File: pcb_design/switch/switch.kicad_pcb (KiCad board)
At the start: 2 copper layers, 5 parts

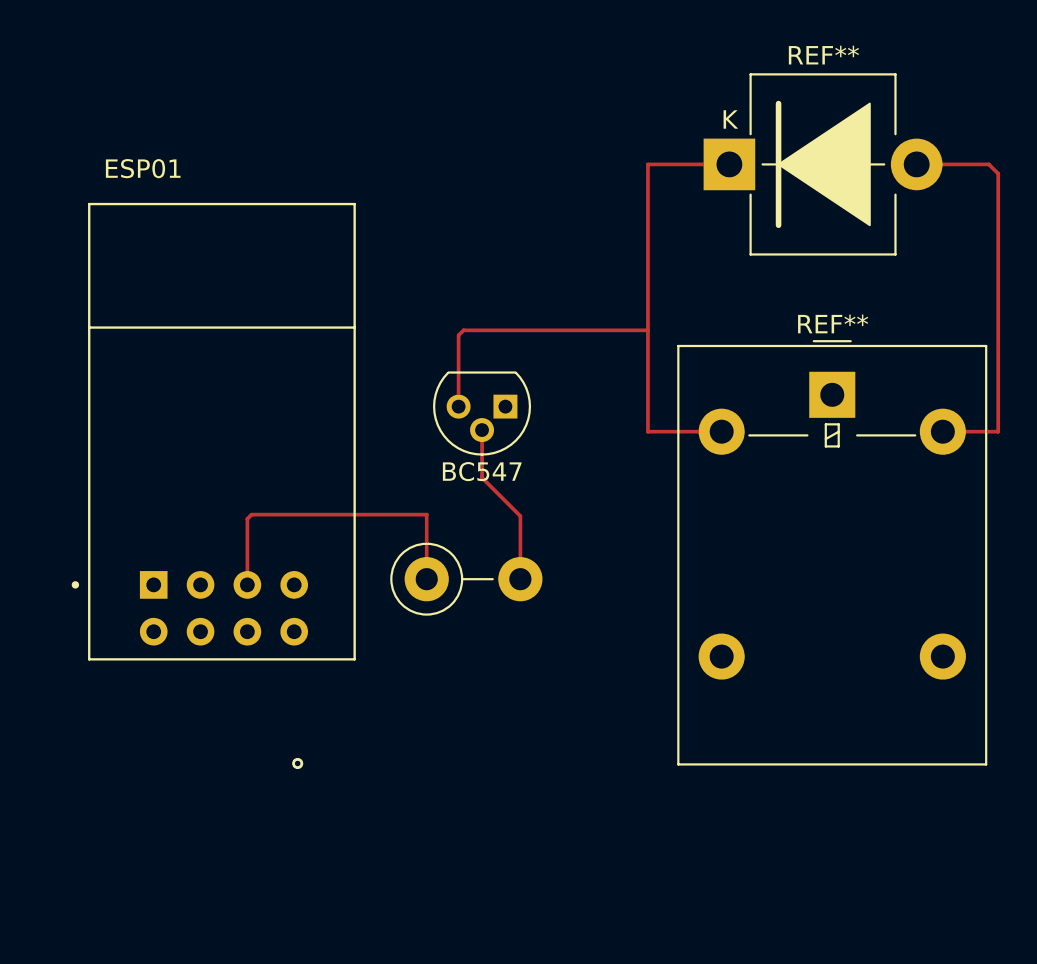
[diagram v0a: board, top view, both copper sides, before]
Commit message: Update fp-info-cache in switch design ``
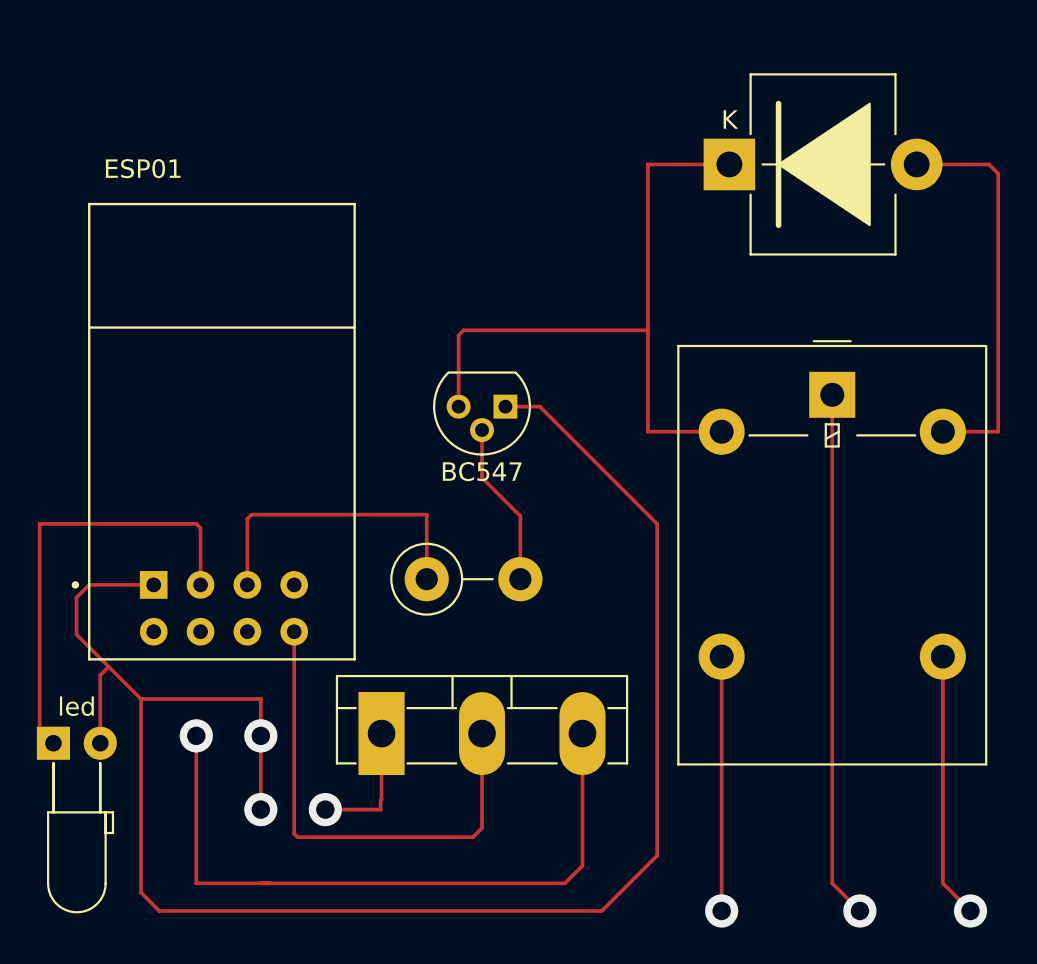
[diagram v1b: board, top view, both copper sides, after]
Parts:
- added REF**: lm1117 3.3, Package_TO_SOT_THT:TO-3P-3_Vertical, F.Cu at (142.6, 101.9)
- added led: LED_D3.0mm_Horizontal_O3.81mm_Z6.0mm, LED_THT:LED_D3.0mm_Horizontal_O3.81mm_Z6.0mm, F.Cu at (124.8, 102.4)
- REF**: value Relay_SPDT_Omron-G5LE-1 -> Relay
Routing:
- net (no net): track 84.7 -> 321.6 mm, vias 1 -> 7

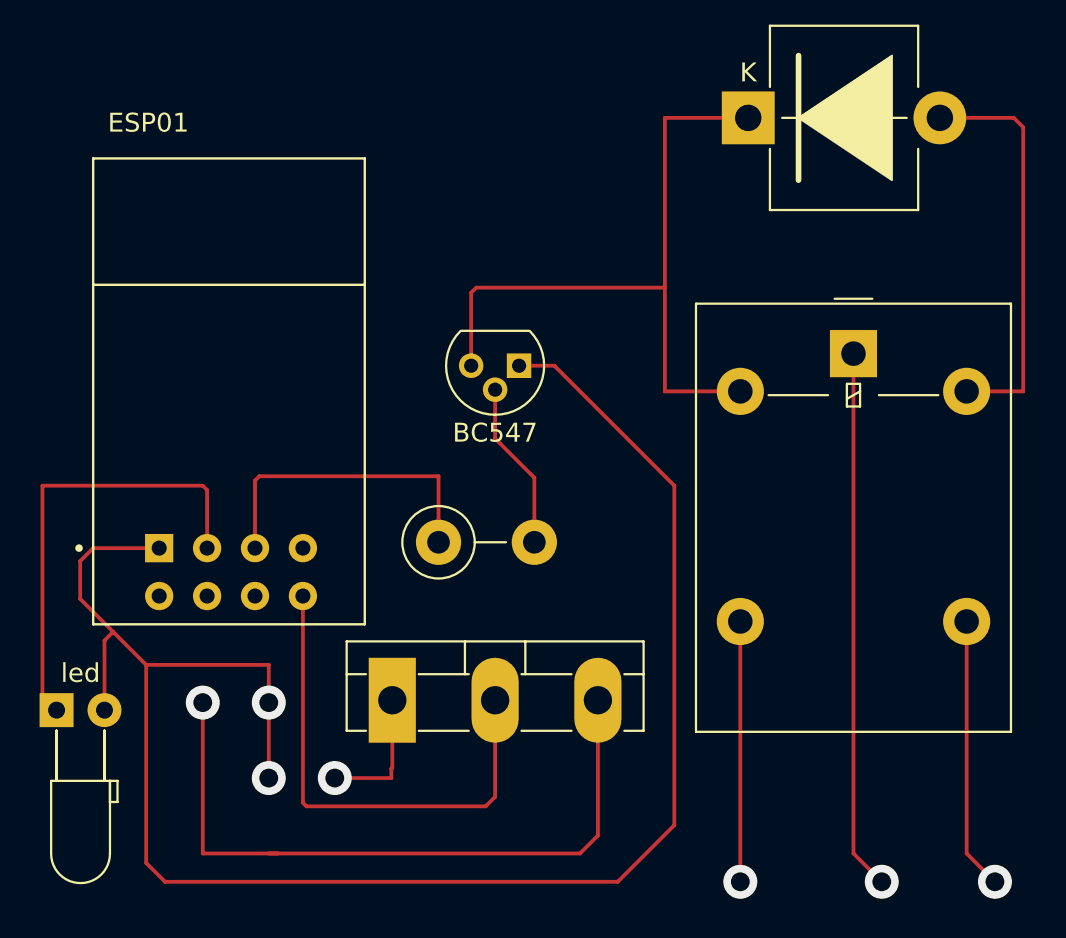
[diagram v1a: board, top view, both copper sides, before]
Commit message: Refactor PCB design files and update switch design dependencies
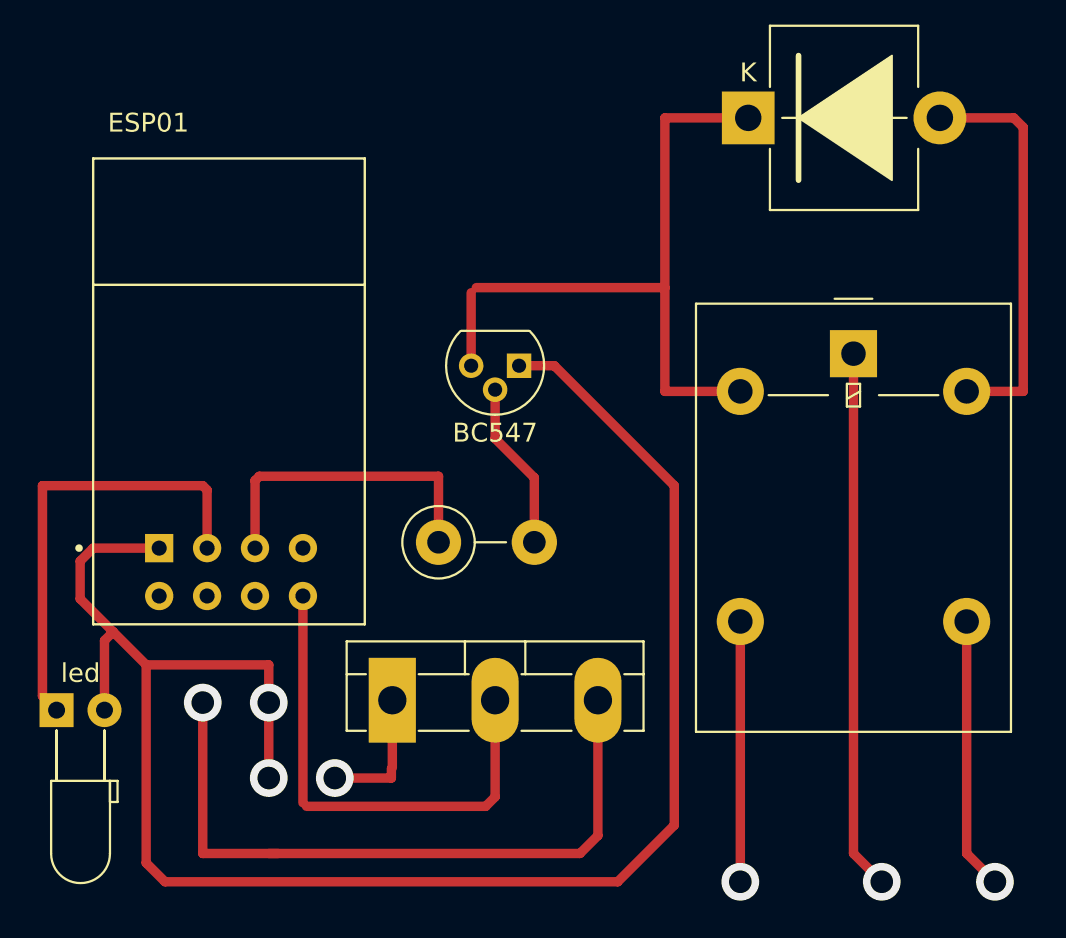
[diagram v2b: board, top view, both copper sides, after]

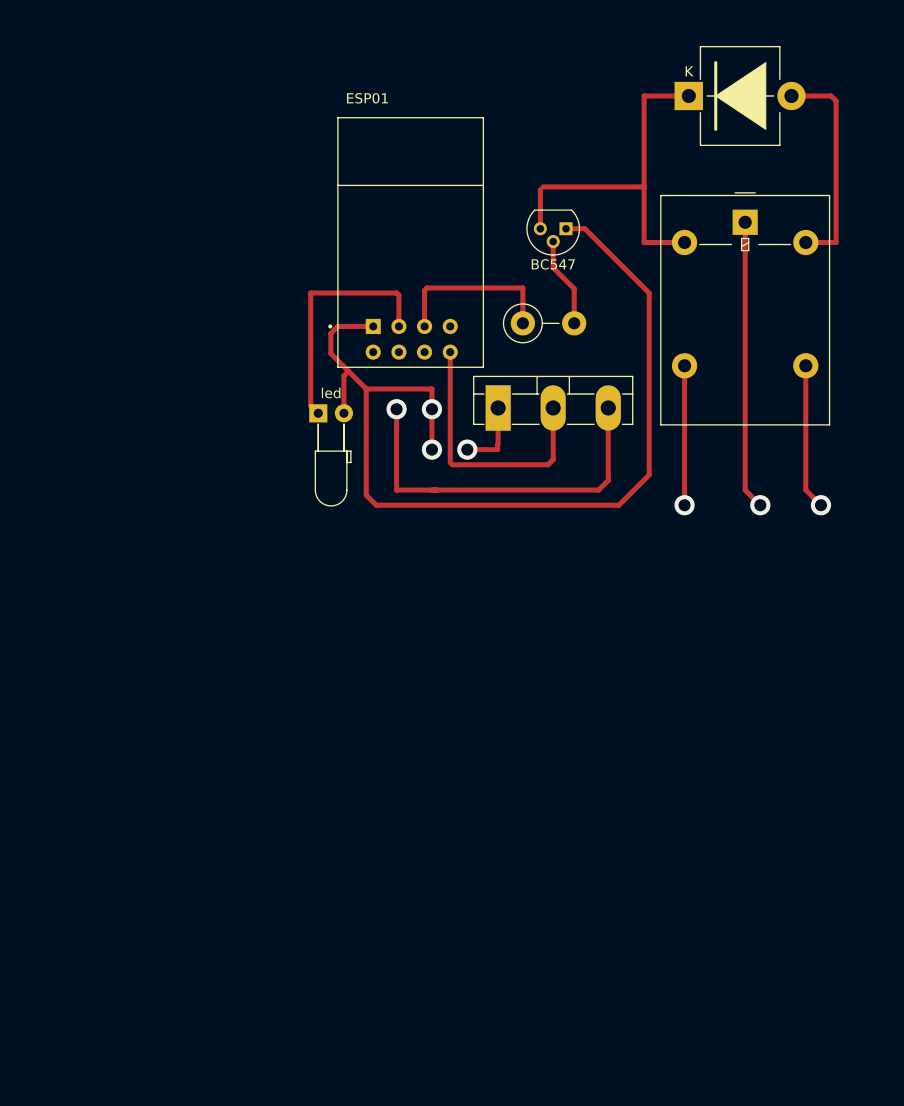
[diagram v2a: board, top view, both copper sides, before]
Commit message: Refactor PCB design files and update switch design dependencies
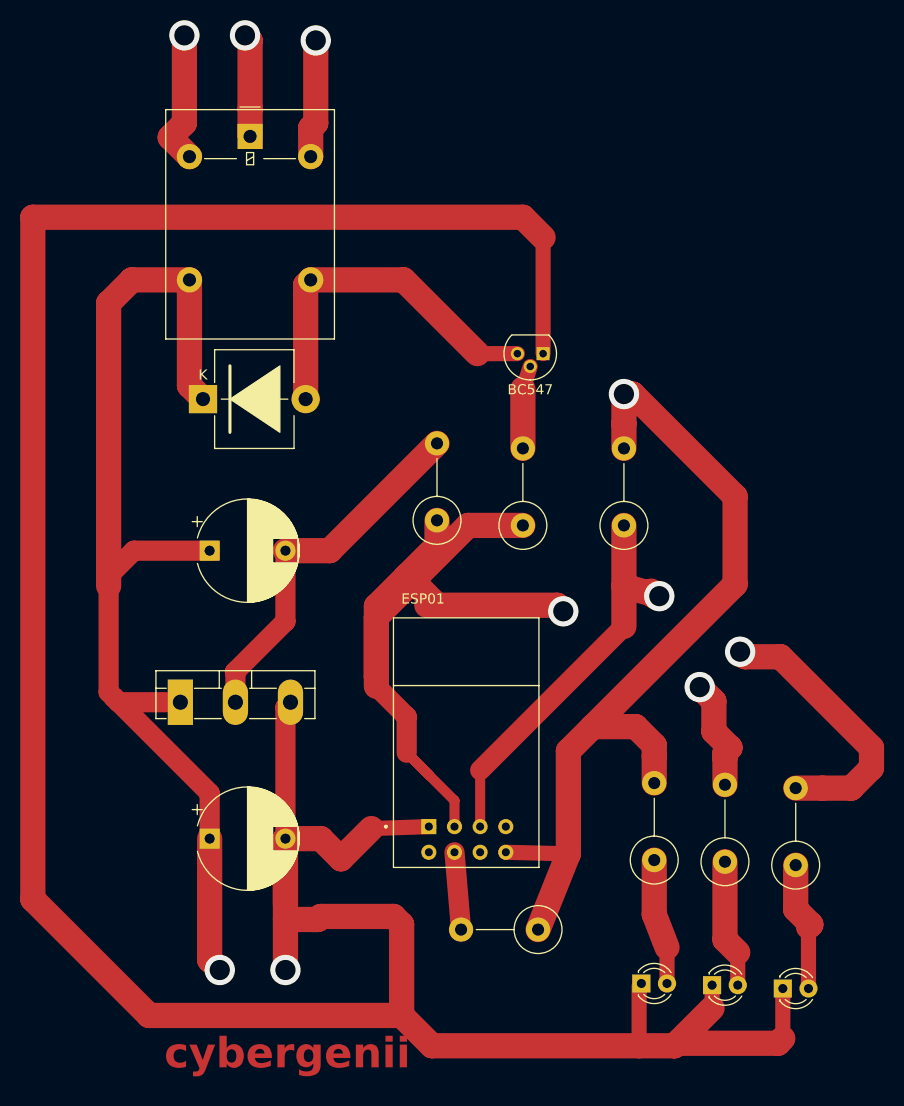
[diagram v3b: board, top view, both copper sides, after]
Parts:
- removed the REF** at (145.0, 93.5)
- removed led: LED_D3.0mm_Horizontal_O3.81mm_Z6.0mm, LED_THT:LED_D3.0mm_Horizontal_O3.81mm_Z6.0mm
- added REF: 10uf, Capacitor_THT:CP_Radial_D10.0mm_P7.50mm, F.Cu at (114.0, 116.0)
- added REF: 10uf, Capacitor_THT:CP_Radial_D10.0mm_P7.50mm, F.Cu at (114.0, 144.5)
- added REF**: 3k3, Resistor_THT:R_Axial_DIN0414_L11.9mm_D4.5mm_P7.62mm_Vertical, F.Cu at (145.0, 113.5)
- added REF**: 3k3, Resistor_THT:R_Axial_DIN0414_L11.9mm_D4.5mm_P7.62mm_Vertical, F.Cu at (146.5, 153.5)
- added REF**: led 1, LED_THT:LED_D3.0mm_Clear, F.Cu at (170.7, 159.3)
- added REF**: led 1, LED_THT:LED_D3.0mm_Clear, F.Cu at (163.7, 159.0)
- added REF**: 3k3, Resistor_THT:R_Axial_DIN0414_L11.9mm_D4.5mm_P7.62mm_Vertical, F.Cu at (155.0, 113.5)
- added REF**: 3k3, Resistor_THT:R_Axial_DIN0414_L11.9mm_D4.5mm_P7.62mm_Vertical, F.Cu at (136.5, 113.0)
- added REF**: 3k3, Resistor_THT:R_Axial_DIN0414_L11.9mm_D4.5mm_P7.62mm_Vertical, F.Cu at (165.0, 146.8)
- added REF**: led 1, LED_THT:LED_D3.0mm_Clear, F.Cu at (156.7, 158.8)
- added REF**: 3k3, Resistor_THT:R_Axial_DIN0414_L11.9mm_D4.5mm_P7.62mm_Vertical, F.Cu at (158.0, 146.6)
- added REF**: 3k3, Resistor_THT:R_Axial_DIN0414_L11.9mm_D4.5mm_P7.62mm_Vertical, F.Cu at (172.0, 147.1)
- moved REF** 56.7 mm to (113.3, 101.0)
- moved ESP01 49.8 mm to (139.5, 135.0)
- moved REF** 49.7 mm to (118.0, 75.0)
- moved REF** 42.9 mm to (111.1, 131.0)
- moved BC547 12.6 mm to (147.0, 96.5)
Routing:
- net (no net): track 321.6 -> 817.4 mm, vias 7 -> 10
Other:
- board text added: "cybergenii"
